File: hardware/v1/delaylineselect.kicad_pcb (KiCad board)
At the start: 2 copper layers, 4 parts, among them P1 CONN_02X02, SW1 SW_PUSH, SW2 Coded_Switch, U1 MCP23017

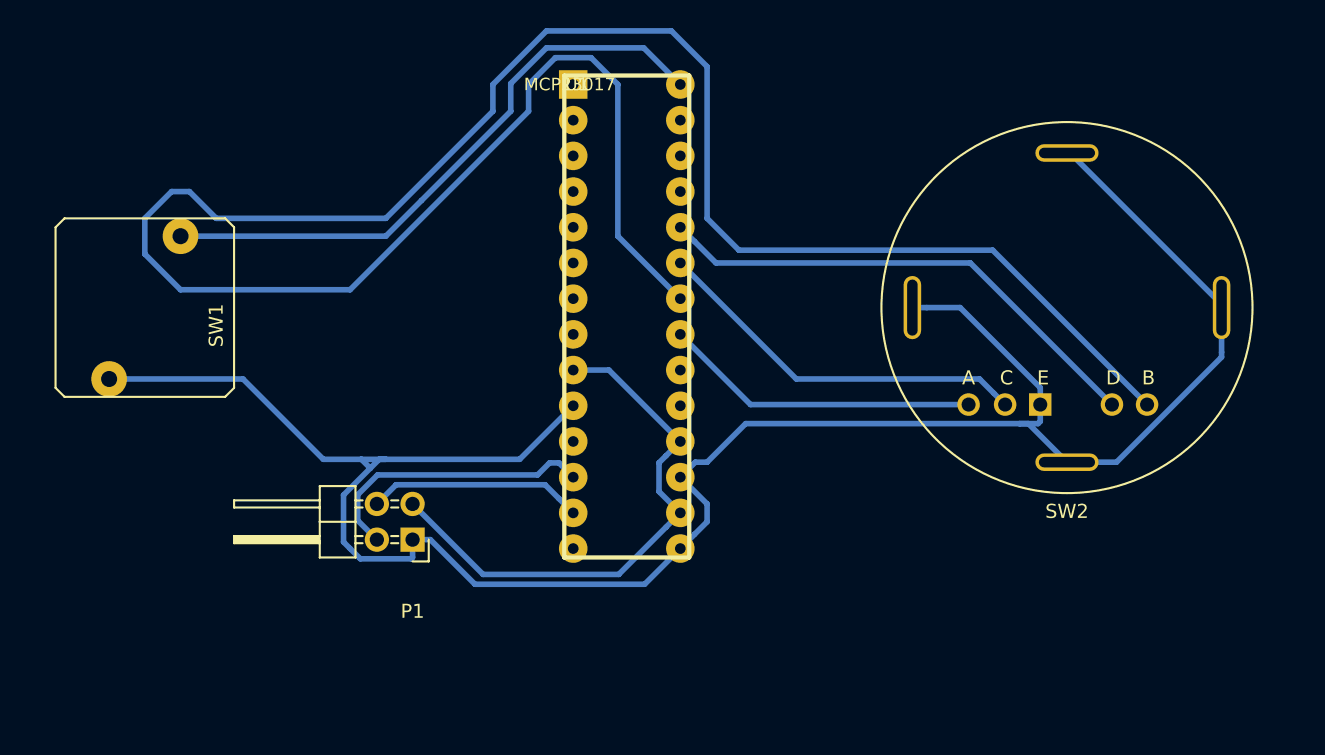
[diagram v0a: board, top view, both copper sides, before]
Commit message: Simplify routing for delaylineselect, generate gerber files and svg.
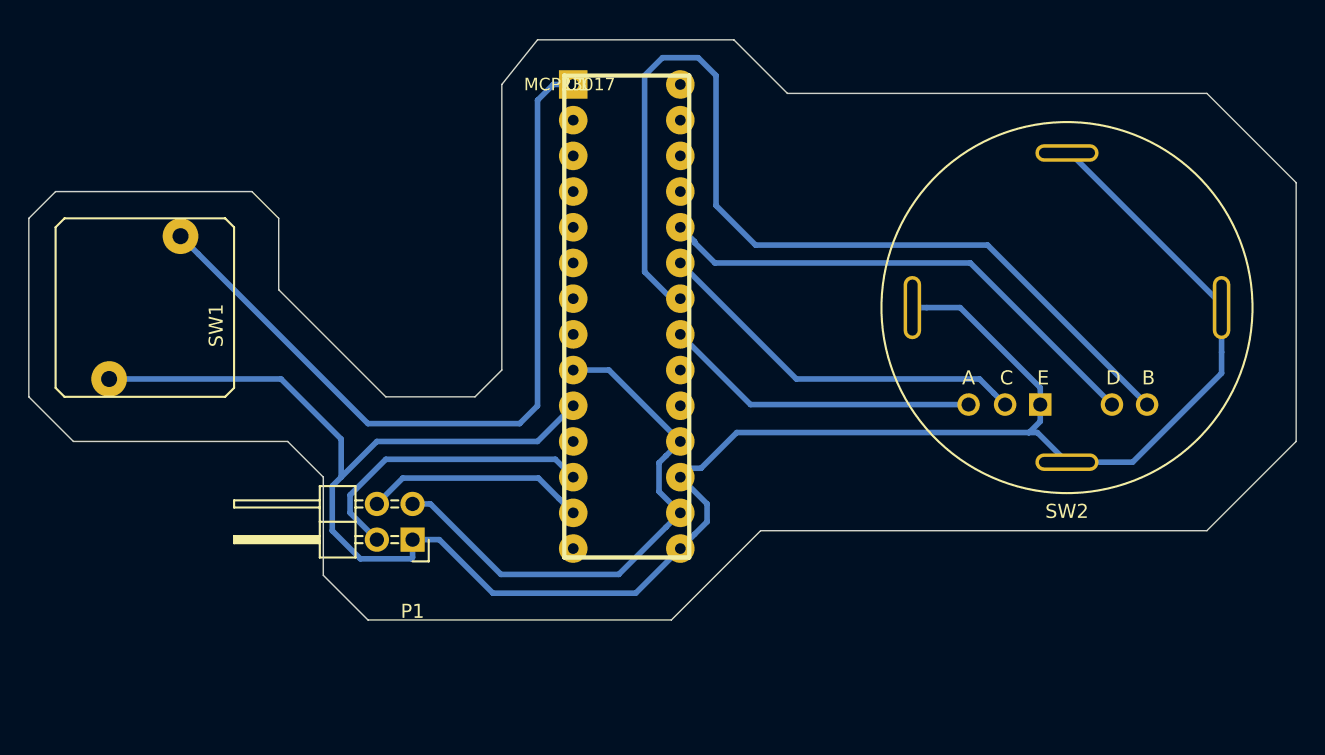
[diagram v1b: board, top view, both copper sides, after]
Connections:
- U1 pad 1: Net-(U1-Pad1) -> /MCSLIP
- U1 pad 28: /MCSLIP -> Net-(U1-Pad28)
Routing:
- net /SELECT_B: track 159.9 -> 69.2 mm
- net /MCSLIP: track 43.3 -> 56.2 mm
- net /SCK: track 20.5 -> 21.4 mm
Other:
- board outline added: 90.2 x 41.3 mm

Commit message: Re-arrange switch connector pinout to simpler single-row header. Re-route the switch boards accordingly.
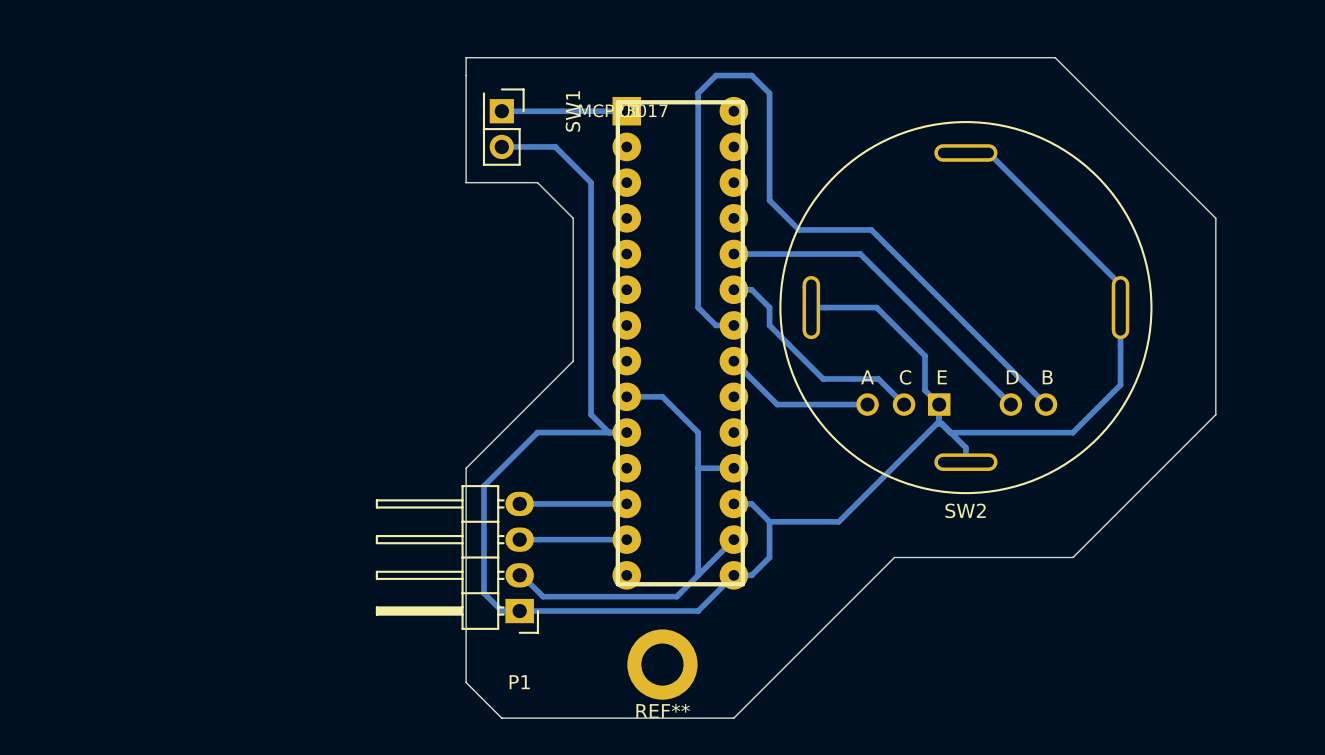
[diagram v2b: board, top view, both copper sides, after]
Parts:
- added REF**: M3, myparts:HOLE_M3, F.Cu at (118.1, 88.9)
- P1: value CONN_02X02 -> CONN_01X04; footprint Pin_Headers:Pin_Header_Angled_2x02 -> Pin_Headers:Pin_Header_Angled_1x04
- SW1: footprint Buttons_Switches_ThroughHole:SW_PUSH -> Pin_Headers:Pin_Header_Straight_2x01
- moved SW1 29.0 mm to (106.7, 49.5)
- moved P1 9.16 mm to (108.0, 85.1)
- moved SW2 7.19 mm to (139.7, 63.5)
- moved U1 4.26 mm to (115.6, 49.5)
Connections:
- P1 pad 2: /SCK -> VDD
- P1 pad 3: VDD -> /SDA
- P1 pad 4: /SDA -> /SCK
- U1 pad 11: Net-(U1-Pad11) -> (no net)
- U1 pad 14: Net-(U1-Pad14) -> (no net)
- U1 pad 19: Net-(U1-Pad19) -> (no net)
- U1 pad 2: Net-(U1-Pad2) -> (no net)
- U1 pad 20: Net-(U1-Pad20) -> (no net)
- U1 pad 25: Net-(U1-Pad25) -> (no net)
- U1 pad 26: Net-(U1-Pad26) -> (no net)
- U1 pad 27: Net-(U1-Pad27) -> (no net)
- U1 pad 28: Net-(U1-Pad28) -> (no net)
- U1 pad 3: Net-(U1-Pad3) -> (no net)
- U1 pad 4: Net-(U1-Pad4) -> (no net)
- U1 pad 5: Net-(U1-Pad5) -> (no net)
- U1 pad 6: Net-(U1-Pad6) -> (no net)
- U1 pad 7: Net-(U1-Pad7) -> (no net)
- U1 pad 8: Net-(U1-Pad8) -> (no net)
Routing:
- net /MCSLIP: track 56.2 -> 8.89 mm
- net /SCK: track 21.4 -> 7.62 mm
- net GND: track 160.5 -> 147.3 mm
- net /SELECT_A: track 22.6 -> 10.8 mm
- net /SELECT_B: track 69.2 -> 57.7 mm
- net /SELECT_C: track 27.3 -> 16.2 mm
- net /SELECT_D: track 36.0 -> 25.3 mm
- net /SDA: track 15.8 -> 7.62 mm
- net VDD: track 39.0 -> 36.4 mm
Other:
- board size 90.2 x 41.3 mm -> 53.3 x 47 mm

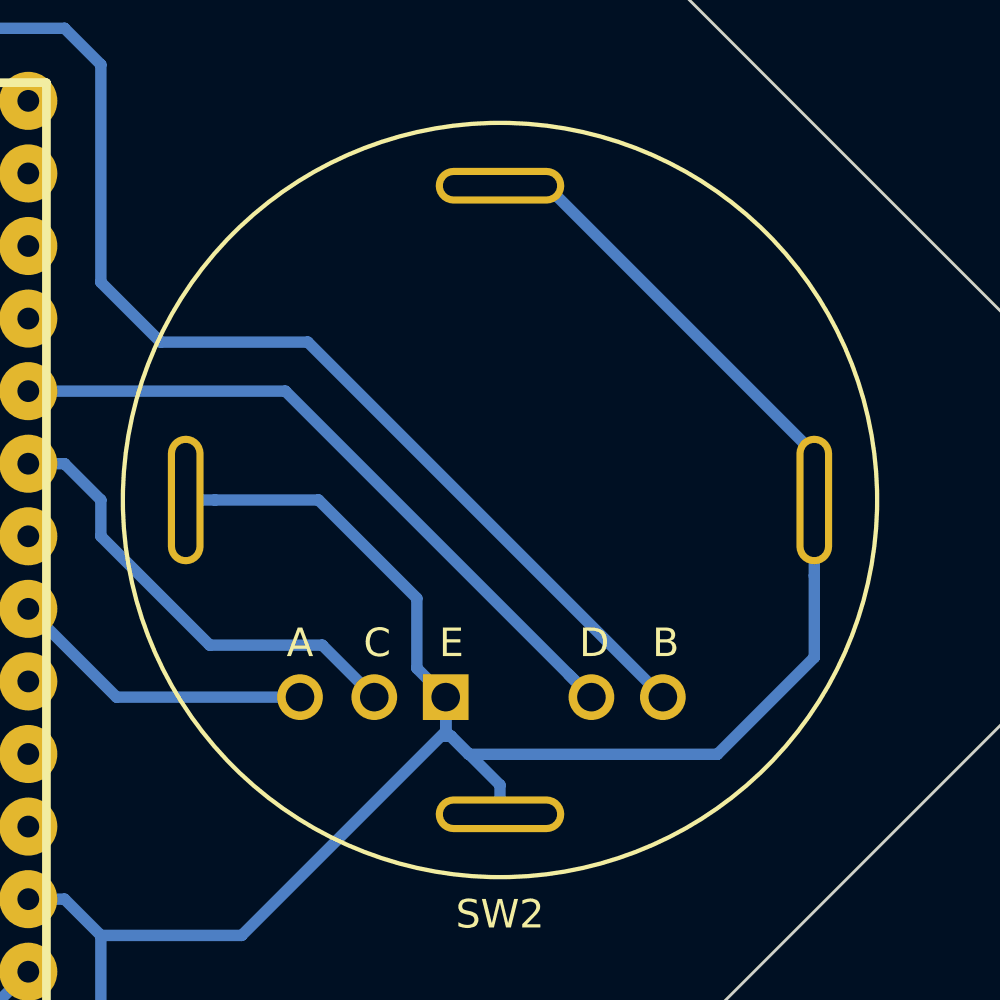
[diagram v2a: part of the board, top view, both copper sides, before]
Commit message: Correct footprints for barrel connector and rotary switch.
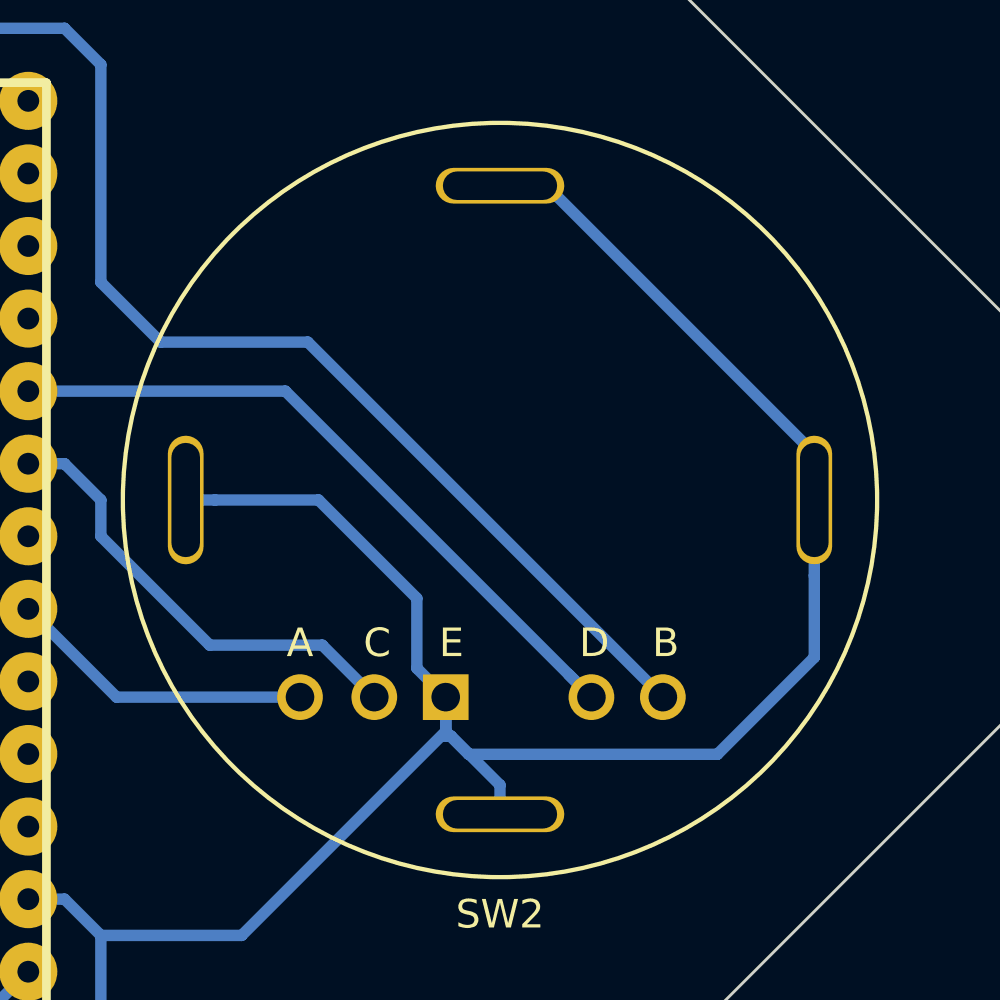
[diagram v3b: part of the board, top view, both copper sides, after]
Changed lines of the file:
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@@
 (kicad_pcb (version 4) (host pcbnew 4.0.2-stable)
   (general
-    (links 0)
+    (links 19)
     (no_connects 0)
-    (area 58.42 31.44 157.530001 91.265)
+    (area 58.42 31.44 157.530001 93.325)
     (thickness 1.6)
     (drawings 18)
@@
     (add_net VDD)
   )
-  (module myparts:ROTARY_BCK1002-custom (layer F.Cu)
-    (at 139.7 63.5)
-    (fp_text reference SW2 (at 0 14.5) (layer F.SilkS)
-      (effects (font (size 1 1) (thickness 0.15)))
-    )
-    (fp_text value Coded_Switch (at 0 -6) (layer F.Fab)
-      (effects (font (size 1 1) (thickness 0.15)))
-    )
-    (fp_text user A (at -7 5) (layer F.SilkS)
-      (effects (font (size 1 1) (thickness 0.15)))
-    )
-    (fp_text user C (at -4.3 5) (layer F.SilkS)
-      (effects (font (size 1 1) (thickness 0.15)))
-    )
-    (fp_text user E (at -1.7 5) (layer F.SilkS)
-      (effects (font (size 1 1) (thickness 0.15)))
-    )
-    (fp_text user D (at 3.3 5) (layer F.SilkS)
-      (effects (font (size 1 1) (thickness 0.15)))
-    )
-    (fp_text user B (at 5.8 5) (layer F.SilkS)
-      (effects (font (size 1 1) (thickness 0.15)))
-    )
-    (fp_circle (center 0 0) (end 13.2 0) (layer F.SilkS) (width 0.15))
-    (fp_circle (center 0 0) (end 5 0) (layer B.Fab) (width 0.15))
-    (pad 1 thru_hole oval (at 0 -11) (size 4.5 1.25) (drill oval 4 0.75) (layers *.Cu *.Mask F.SilkS)
-      (net 1 GND))
-    (pad 1 thru_hole oval (at 0 11) (size 4.5 1.25) (drill oval 4 0.75) (layers *.Cu *.Mask F.SilkS)
-      (net 1 GND))
-    (pad 1 thru_hole oval (at 11 0 90) (size 4.5 1.25) (drill oval 4 0.75) (layers *.Cu *.Mask F.SilkS)
-      (net 1 GND))
-    (pad 1 thru_hole oval (at -11 0 90) (size 4.5 1.25) (drill oval 4 0.75) (layers *.Cu *.Mask F.SilkS)
-      (net 1 GND))
-    (pad 1 thru_hole rect (at -1.9 6.9) (size 1.6 1.6) (drill 1) (layers *.Cu *.Mask F.SilkS)
-      (net 1 GND))
-    (pad 4 thru_hole circle (at -4.4 6.9) (size 1.6 1.6) (drill 1) (layers *.Cu *.Mask F.SilkS)
-      (net 6 /SELECT_C))
-    (pad 2 thru_hole circle (at -7 6.9) (size 1.6 1.6) (drill 1) (layers *.Cu *.Mask F.SilkS)
-      (net 7 /SELECT_A))
-    (pad 5 thru_hole circle (at 3.2 6.9) (size 1.6 1.6) (drill 1) (layers *.Cu *.Mask F.SilkS)
-      (net 8 /SELECT_D))
-    (pad 3 thru_hole circle (at 5.7 6.9) (size 1.6 1.6) (drill 1) (layers *.Cu *.Mask F.SilkS)
-      (net 9 /SELECT_B))
-  )
   (module DIL28:DIL28 (layer F.Cu)
     (at 115.57 49.53 270)
@@
     (pad 1 thru_hole circle (at 0 0) (size 5 5) (drill 3) (layers *.Cu *.Mask F.SilkS))
   )
+  (module myparts:ROTARY_BCK1002-custom (layer F.Cu)
+    (at 139.7 63.5)
+    (fp_text reference SW2 (at 0 14.5) (layer F.SilkS)
+      (effects (font (size 1 1) (thickness 0.15)))
+    )
+    (fp_text value Coded_Switch (at 0 -6) (layer F.Fab)
+      (effects (font (size 1 1) (thickness 0.15)))
+    )
+    (fp_text user A (at -7 5) (layer F.SilkS)
+      (effects (font (size 1 1) (thickness 0.15)))
+    )
+    (fp_text user C (at -4.3 5) (layer F.SilkS)
+      (effects (font (size 1 1) (thickness 0.15)))
+    )
+    (fp_text user E (at -1.7 5) (layer F.SilkS)
+      (effects (font (size 1 1) (thickness 0.15)))
+    )
+    (fp_text user D (at 3.3 5) (layer F.SilkS)
+      (effects (font (size 1 1) (thickness 0.15)))
+    )
+    (fp_text user B (at 5.8 5) (layer F.SilkS)
+      (effects (font (size 1 1) (thickness 0.15)))
+    )
+    (fp_circle (center 0 0) (end 13.2 0) (layer F.SilkS) (width 0.15))
+    (fp_circle (center 0 0) (end 5 0) (layer B.Fab) (width 0.15))
+    (pad 1 thru_hole oval (at 0 -11) (size 4.5 1.25) (drill oval 4 1) (layers *.Cu *.Mask F.SilkS)
+      (net 1 GND))
+    (pad 1 thru_hole oval (at 0 11) (size 4.5 1.25) (drill oval 4 1) (layers *.Cu *.Mask F.SilkS)
+      (net 1 GND))
+    (pad 1 thru_hole oval (at 11 0 90) (size 4.5 1.25) (drill oval 4 1) (layers *.Cu *.Mask F.SilkS)
+      (net 1 GND))
+    (pad 1 thru_hole oval (at -11 0 90) (size 4.5 1.25) (drill oval 4 1) (layers *.Cu *.Mask F.SilkS)
+      (net 1 GND))
+    (pad 1 thru_hole rect (at -1.9 6.9) (size 1.6 1.6) (drill 1) (layers *.Cu *.Mask F.SilkS)
+      (net 1 GND))
+    (pad 4 thru_hole circle (at -4.4 6.9) (size 1.6 1.6) (drill 1) (layers *.Cu *.Mask F.SilkS)
+      (net 6 /SELECT_C))
+    (pad 2 thru_hole circle (at -7 6.9) (size 1.6 1.6) (drill 1) (layers *.Cu *.Mask F.SilkS)
+      (net 7 /SELECT_A))
+    (pad 5 thru_hole circle (at 3.2 6.9) (size 1.6 1.6) (drill 1) (layers *.Cu *.Mask F.SilkS)
+      (net 8 /SELECT_D))
+    (pad 3 thru_hole circle (at 5.7 6.9) (size 1.6 1.6) (drill 1) (layers *.Cu *.Mask F.SilkS)
+      (net 9 /SELECT_B))
+  )
   (gr_line (start 104.14 45.72) (end 104.14 46.99) (layer Edge.Cuts) (width 0.1))
